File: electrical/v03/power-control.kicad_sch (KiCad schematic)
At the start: 28 parts, among them J202 12V STANDBY INPUT, U2 NE5532, U3 NE5532

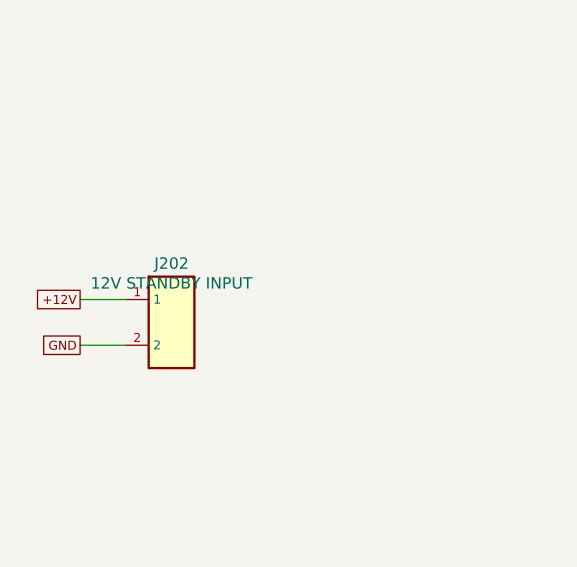
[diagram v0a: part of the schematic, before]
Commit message: Plan internal dual supplies with a single mains inlet
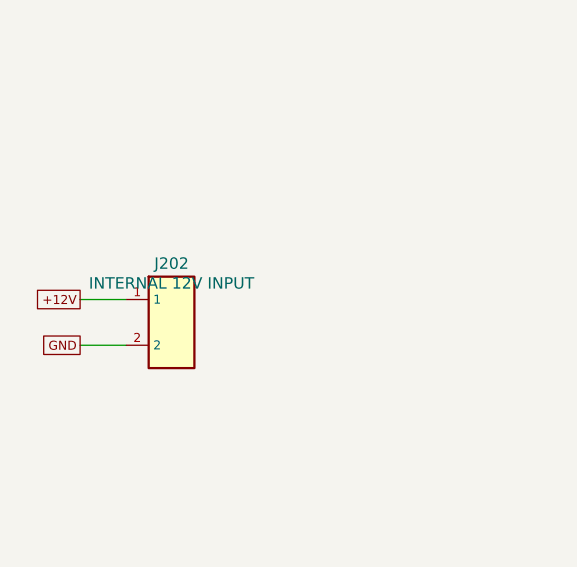
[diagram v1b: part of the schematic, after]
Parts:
- J202: value 12V STANDBY INPUT -> INTERNAL 12V INPUT
